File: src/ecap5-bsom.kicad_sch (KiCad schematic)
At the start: 0 parts

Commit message: Starts adding the power schematics
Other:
- added sheet Power (power.kicad_sch)
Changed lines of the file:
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@@
 		(comment 3 "${Part Number}")
+	)
+	(sheet
+		(at 203.2 95.25)
+		(size 35.56 26.67)
+		(fields_autoplaced yes)
+		(stroke
+			(width 0.1524)
+			(type solid)
+		)
+		(fill
+			(color 0 0 0 0.0000)
+		)
+		(property "Sheetname" "Power"
+			(at 203.2 94.5384 0)
+			(effects
+				(font
+					(size 1.27 1.27)
+				)
+				(justify left bottom)
+			)
+		)
+		(property "Sheetfile" "power.kicad_sch"
+			(at 203.2 122.5046 0)
+			(effects
+				(font
+					(size 1.27 1.27)
+				)
+				(justify left top)
+			)
+		)
+		(instances
+			(project "ecap5-bsom"
+				(path "/c5fd18a3-9aa0-4151-b6e0-94da3d606686"
+					(page "2")
+				)
+			)
+		)
 	)
 	(sheet_instances

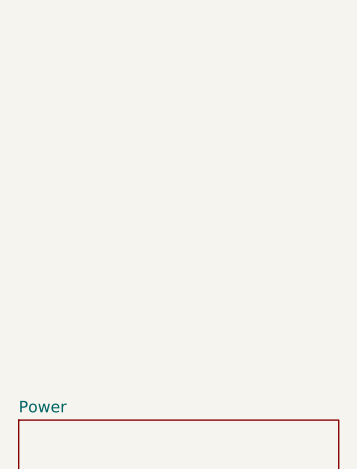
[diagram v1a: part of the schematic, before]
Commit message: Adds io connector symbol
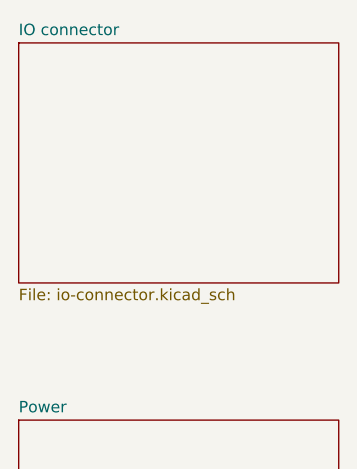
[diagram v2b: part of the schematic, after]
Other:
- added sheet IO connector (io-connector.kicad_sch)
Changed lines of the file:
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@@
+	)
+	(sheet
+		(at 203.2 53.34)
+		(size 35.56 26.67)
+		(fields_autoplaced yes)
+		(stroke
+			(width 0.1524)
+			(type solid)
+		)
+		(fill
+			(color 0 0 0 0.0000)
+		)
+		(property "Sheetname" "IO connector"
+			(at 203.2 52.6284 0)
+			(effects
+				(font
+					(size 1.27 1.27)
+				)
+				(justify left bottom)
+			)
+		)
+		(property "Sheetfile" "io-connector.kicad_sch"
+			(at 203.2 80.5946 0)
+			(effects
+				(font
+					(size 1.27 1.27)
+				)
+				(justify left top)
+			)
+		)
+		(instances
+			(project "ecap5-bsom"
+				(path "/c5fd18a3-9aa0-4151-b6e0-94da3d606686"
+					(page "3")
+				)
+			)
+		)
 	)
 	(sheet

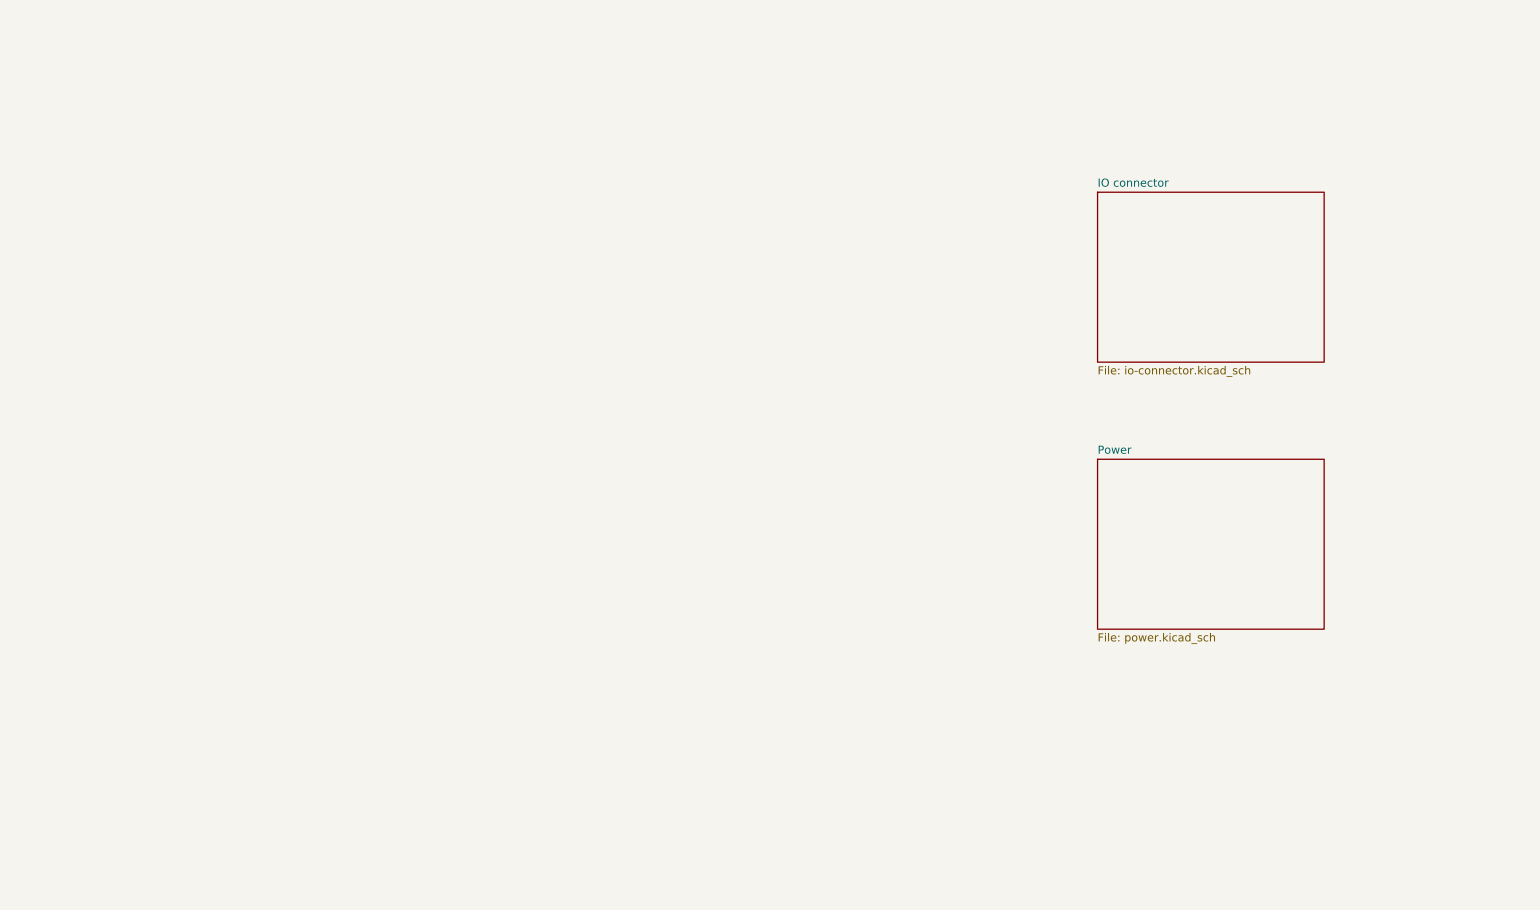
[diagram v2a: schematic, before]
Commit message: Adds schematic for the io connector
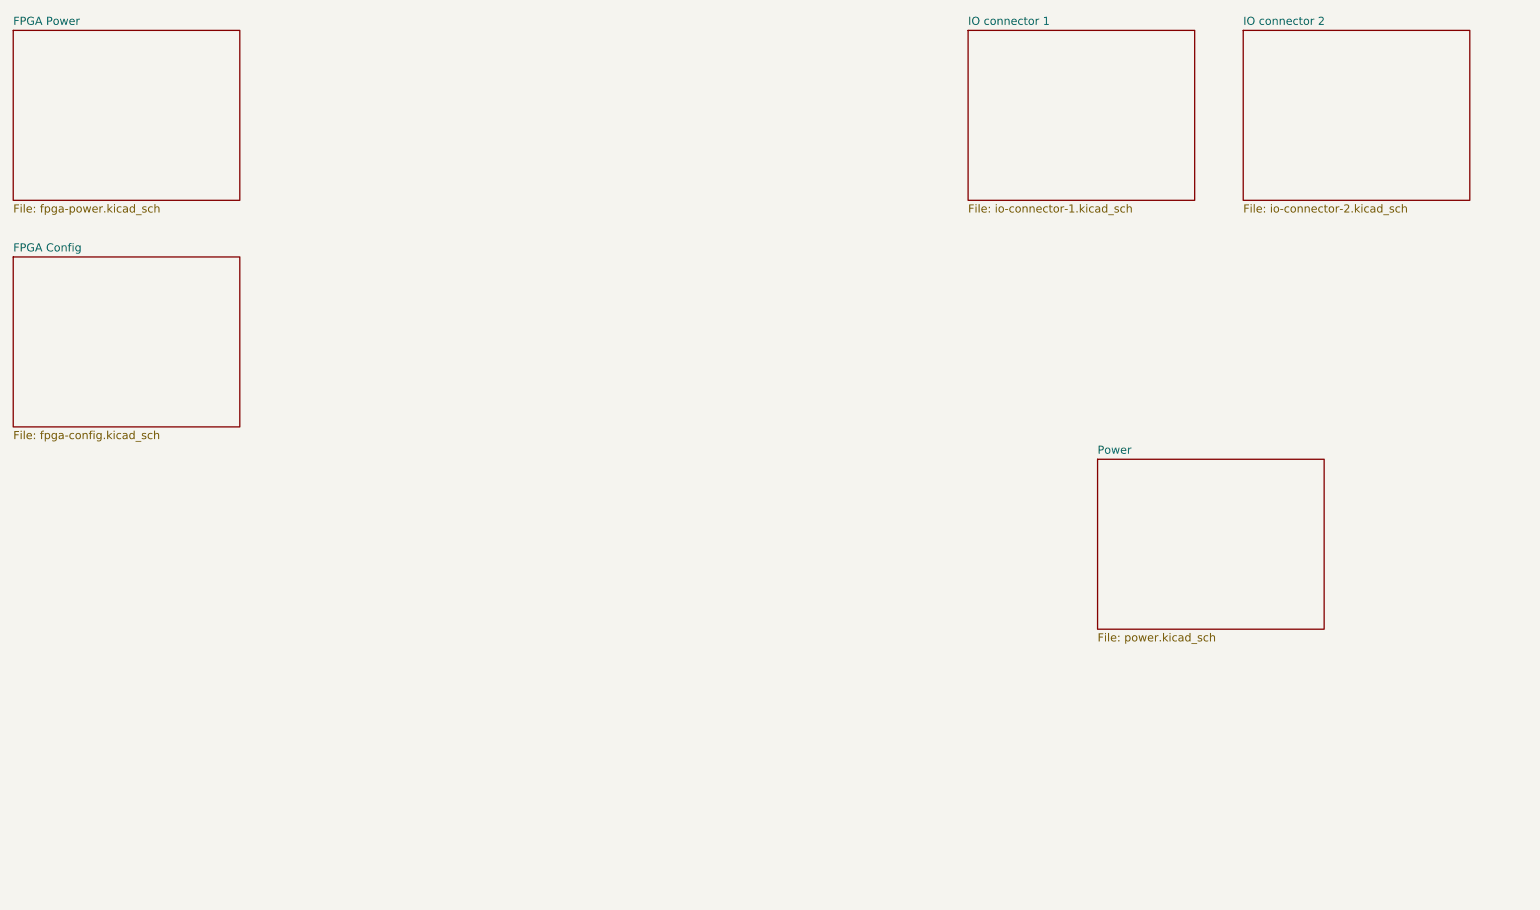
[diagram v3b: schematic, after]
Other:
- sheet IO connector renamed IO connector 1
- added sheet FPGA Config (fpga-config.kicad_sch)
- added sheet FPGA Power (fpga-power.kicad_sch)
- added sheet IO connector 2 (io-connector-2.kicad_sch)
- sheet IO connector 1: file io-connector.kicad_sch -> io-connector-1.kicad_sch
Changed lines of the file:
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@@
 	)
 	(sheet
-		(at 203.2 53.34)
+		(at 226.06 27.94)
 		(size 35.56 26.67)
 		(fields_autoplaced yes)
@@
 			(color 0 0 0 0.0000)
 		)
-		(property "Sheetname" "IO connector"
-			(at 203.2 52.6284 0)
+		(property "Sheetname" "IO connector 2"
+			(at 226.06 27.2284 0)
 			(effects
 				(font
@@
 			)
 		)
-		(property "Sheetfile" "io-connector.kicad_sch"
-			(at 203.2 80.5946 0)
+		(property "Sheetfile" "io-connector-2.kicad_sch"
+			(at 226.06 55.1946 0)
 			(effects
 				(font
@@
 			(project "ecap5-bsom"
 				(path "/c5fd18a3-9aa0-4151-b6e0-94da3d606686"
-					(page "3")
+					(page "5")
+				)
+			)
+		)
+	)
+	(sheet
+		(at 182.88 27.94)
+		(size 35.56 26.67)
+		(fields_autoplaced yes)
+		(stroke
+			(width 0.1524)
+			(type solid)
+		)
+		(fill
+			(color 0 0 0 0.0000)
+		)
+		(property "Sheetname" "IO connector 1"
+			(at 182.88 27.2284 0)
+			(effects
+				(font
+					(size 1.27 1.27)
+				)
+				(justify left bottom)
+			)
+		)
+		(property "Sheetfile" "io-connector-1.kicad_sch"
+			(at 182.88 55.1946 0)
+			(effects
+				(font
+					(size 1.27 1.27)
+				)
+				(justify left top)
+			)
+		)
+		(instances
+			(project "ecap5-bsom"
+				(path "/c5fd18a3-9aa0-4151-b6e0-94da3d606686"
+					(page "4")
 				)
 			)
@@
 				)
 			)
+		)
+	)
+	(sheet
+		(at 33.02 63.5)
+		(size 35.56 26.67)
+		(fields_autoplaced yes)
+		(stroke
+			(width 0.1524)
+			(type solid)
+		)
+		(fill
+			(color 0 0 0 0.0000)
+		)
+		(property "Sheetname" "FPGA Config"
+			(at 33.02 62.7884 0)
+			(effects
+				(font
+					(size 1.27 1.27)
+				)
+				(justify left bottom)
+			)
+		)
+		(property "Sheetfile" "fpga-config.kicad_sch"
+			(at 33.02 90.7546 0)
+			(effects
+				(font
+					(size 1.27 1.27)
+				)
+				(justify left top)
+			)
+		)
+		(instances
+			(project "ecap5-bsom"
+				(path "/c5fd18a3-9aa0-4151-b6e0-94da3d606686"
+					(page "6")
+				)
+			)
+		)
+	)
+	(sheet
+		(at 33.02 27.94)
+		(size 35.56 26.67)
+		(fields_autoplaced yes)
+		(stroke
+			(width 0.1524)
+			(type solid)
+		)
+		(fill
+			(color 0 0 0 0.0000)
+		)
+		(property "Sheetname" "FPGA Power"
+			(at 33.02 27.2284 0)
+			(effects
+				(font
+					(size 1.27 1.27)
+				)
+				(justify left bottom)
+			)
+		)
+		(property "Sheetfile" "fpga-power.kicad_sch"
+			(at 33.02 55.1946 0)
+			(effects
+				(font
+					(size 1.27 1.27)
+				)
+				(justify left top)
+			)
+		)
+		(instances
+			(project "ecap5-bsom"
+				(path "/c5fd18a3-9aa0-4151-b6e0-94da3d606686"
+					(page "3")
+				)
+			)

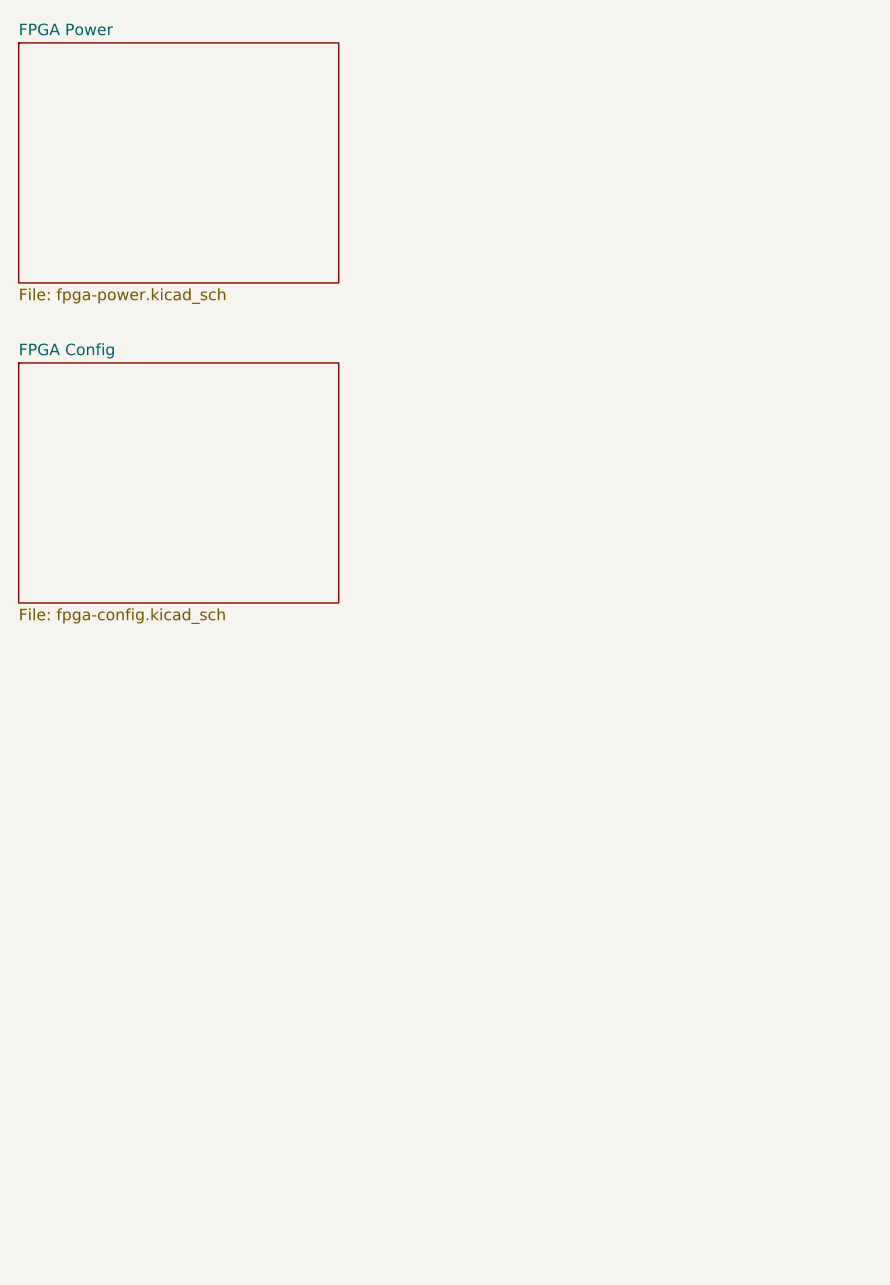
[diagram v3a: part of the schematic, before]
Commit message: Adds more FPGA IO banks
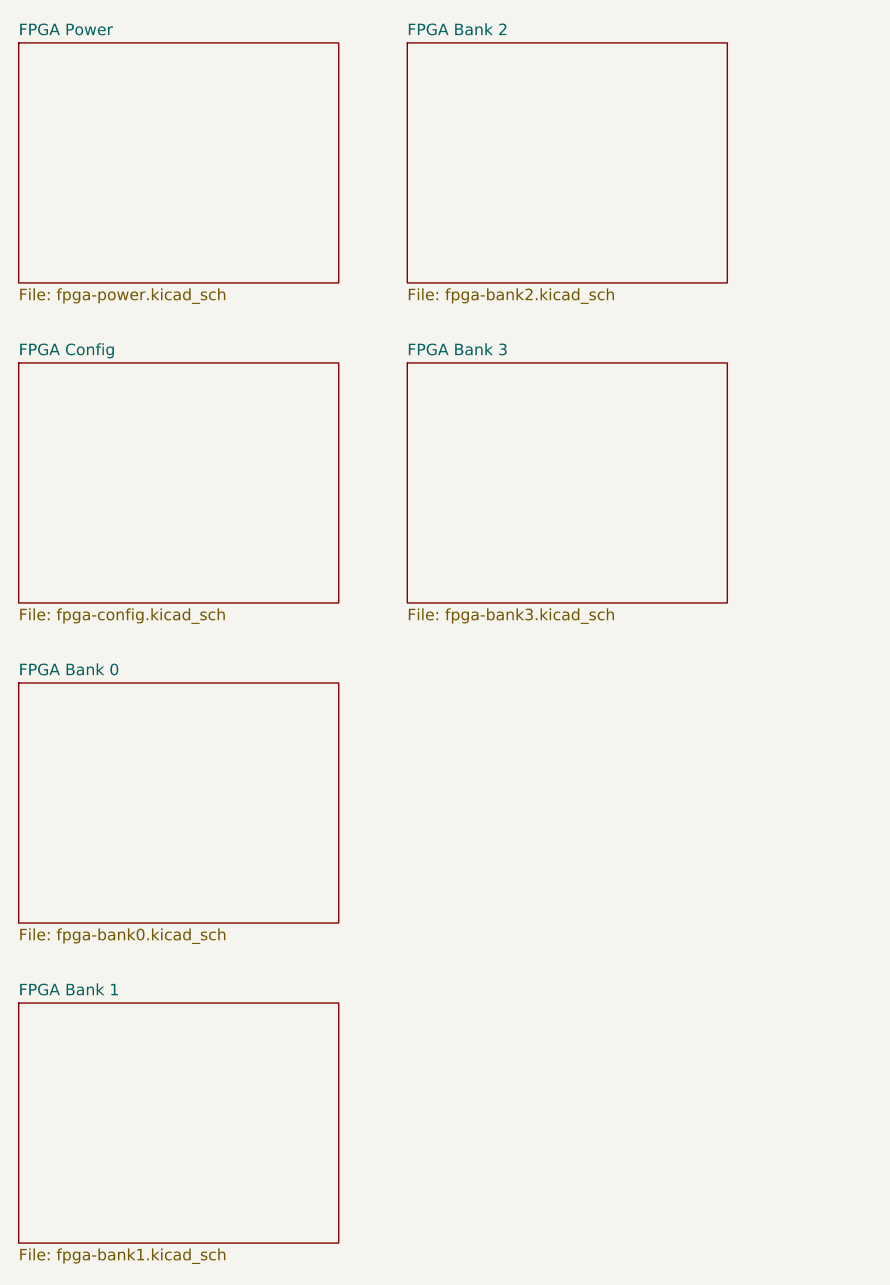
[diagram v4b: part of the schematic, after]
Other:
- added sheet FPGA Bank 0 (fpga-bank0.kicad_sch)
- added sheet FPGA Bank 1 (fpga-bank1.kicad_sch)
- added sheet FPGA Bank 2 (fpga-bank2.kicad_sch)
- added sheet FPGA Bank 3 (fpga-bank3.kicad_sch)
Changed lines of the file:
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@@
+	)
+	(sheet
+		(at 33.02 99.06)
+		(size 35.56 26.67)
+		(fields_autoplaced yes)
+		(stroke
+			(width 0.1524)
+			(type solid)
+		)
+		(fill
+			(color 0 0 0 0.0000)
+		)
+		(property "Sheetname" "FPGA Bank 0"
+			(at 33.02 98.3484 0)
+			(effects
+				(font
+					(size 1.27 1.27)
+				)
+				(justify left bottom)
+			)
+		)
+		(property "Sheetfile" "fpga-bank0.kicad_sch"
+			(at 33.02 126.3146 0)
+			(effects
+				(font
+					(size 1.27 1.27)
+				)
+				(justify left top)
+			)
+		)
+		(instances
+			(project "ecap5-bsom"
+				(path "/c5fd18a3-9aa0-4151-b6e0-94da3d606686"
+					(page "7")
+				)
+			)
+		)
+	)
+	(sheet
+		(at 76.2 63.5)
+		(size 35.56 26.67)
+		(fields_autoplaced yes)
+		(stroke
+			(width 0.1524)
+			(type solid)
+		)
+		(fill
+			(color 0 0 0 0.0000)
+		)
+		(property "Sheetname" "FPGA Bank 3"
+			(at 76.2 62.7884 0)
+			(effects
+				(font
+					(size 1.27 1.27)
+				)
+				(justify left bottom)
+			)
+		)
+		(property "Sheetfile" "fpga-bank3.kicad_sch"
+			(at 76.2 90.7546 0)
+			(effects
+				(font
+					(size 1.27 1.27)
+				)
+				(justify left top)
+			)
+		)
+		(instances
+			(project "ecap5-bsom"
+				(path "/c5fd18a3-9aa0-4151-b6e0-94da3d606686"
+					(page "10")
+				)
+			)
+		)
 	)
 	(sheet
@@
 				)
 			)
+		)
+	)
+	(sheet
+		(at 76.2 27.94)
+		(size 35.56 26.67)
+		(fields_autoplaced yes)
+		(stroke
+			(width 0.1524)
+			(type solid)
+		)
+		(fill
+			(color 0 0 0 0.0000)
+		)
+		(property "Sheetname" "FPGA Bank 2"
+			(at 76.2 27.2284 0)
+			(effects
+				(font
+					(size 1.27 1.27)
+				)
+				(justify left bottom)
+			)
+		)
+		(property "Sheetfile" "fpga-bank2.kicad_sch"
+			(at 76.2 55.1946 0)
+			(effects
+				(font
+					(size 1.27 1.27)
+				)
+				(justify left top)
+			)
+		)
+		(instances
+			(project "ecap5-bsom"
+				(path "/c5fd18a3-9aa0-4151-b6e0-94da3d606686"
+					(page "9")
+				)
+			)
+		)
+	)
+	(sheet
+		(at 33.02 134.62)
+		(size 35.56 26.67)
+		(fields_autoplaced yes)
+		(stroke
+			(width 0.1524)
+			(type solid)
+		)
+		(fill
+			(color 0 0 0 0.0000)
+		)
+		(property "Sheetname" "FPGA Bank 1"
+			(at 33.02 133.9084 0)
+			(effects
+				(font
+					(size 1.27 1.27)
+				)
+				(justify left bottom)
+			)
+		)
+		(property "Sheetfile" "fpga-bank1.kicad_sch"
+			(at 33.02 161.8746 0)
+			(effects
+				(font
+					(size 1.27 1.27)
+				)
+				(justify left top)
+			)
+		)
+		(instances
+			(project "ecap5-bsom"
+				(path "/c5fd18a3-9aa0-4151-b6e0-94da3d606686"
+					(page "8")
+				)
+			)
